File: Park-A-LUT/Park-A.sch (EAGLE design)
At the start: 38 parts, among them Q1 16MHz, T1 BC848SMD, T2 IRLML5203, T3 BC848SMD, T4 IRLML5203, U1 PIC18F25K80, U2 78M05, U3 TJA1055T

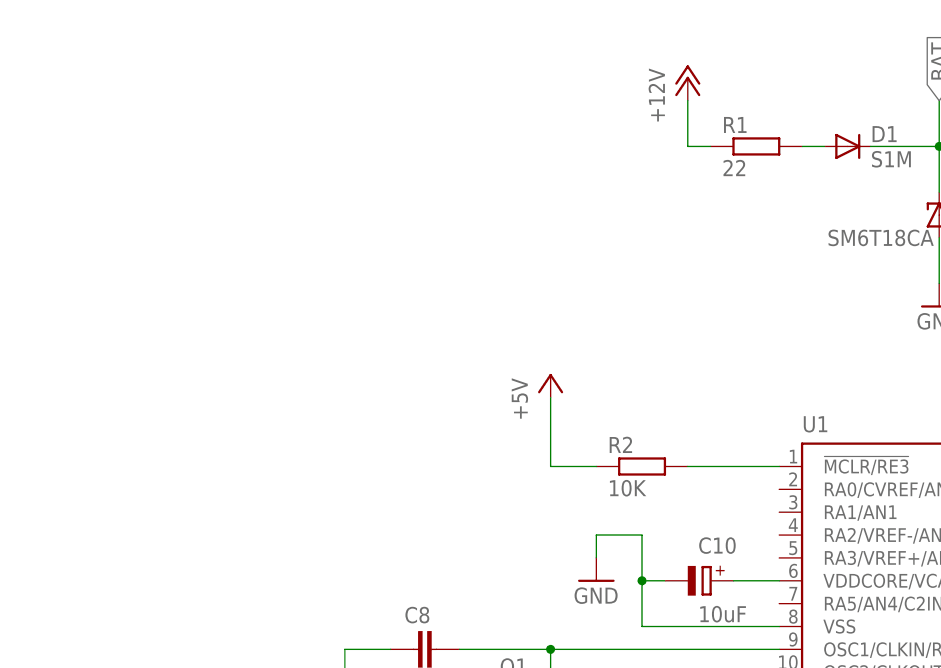
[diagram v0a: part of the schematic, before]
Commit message: Add ICSP
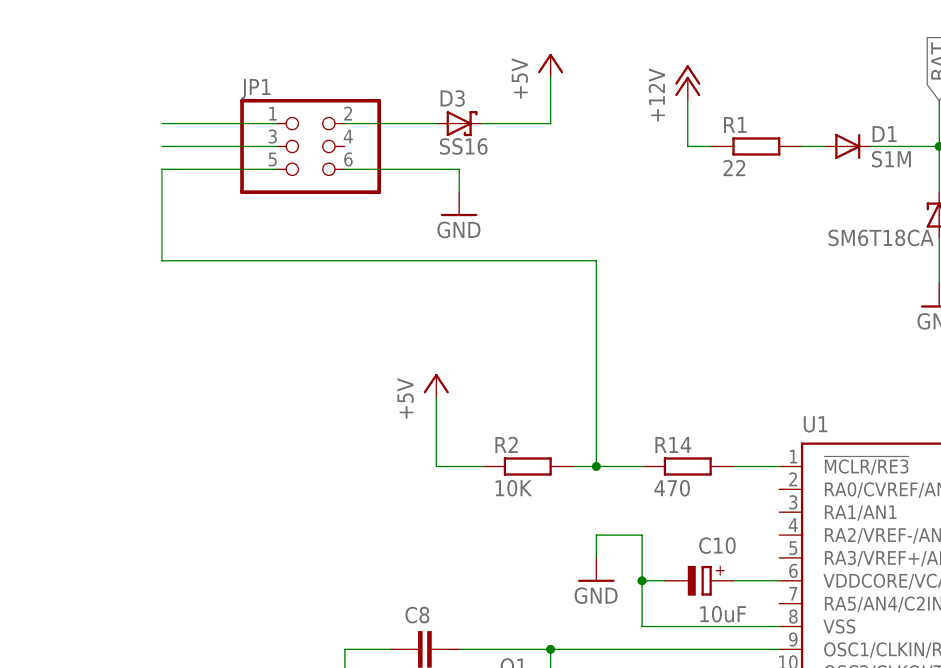
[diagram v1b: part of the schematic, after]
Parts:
- added D3: SS16, Park-A:SS16
- added JP1: (no value), Park-A:PINHD-2X3
- added R14: 470, rcl:R-EU_R0805
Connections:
- new net N$19: JP1.5, R14.1, R2.2
- new net N$20: D3.A, JP1.2
- net +5V: now also D3.C
- net GND: now also JP1.6
- net N$4: now also R14.2; no longer R2.2
- net PGC: now also JP1.1
- net PGD: now also JP1.3
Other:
- moved on the sheet: R2
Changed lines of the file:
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@@
 <part name="T4" library="Park-A" deviceset="IRLML5203" device=""/>
 <part name="GND12" library="supply1" deviceset="GND" device=""/>
+<part name="JP1" library="Park-A" deviceset="PINHD-2X3" device=""/>
+<part name="GND13" library="supply1" deviceset="GND" device=""/>
+<part name="R14" library="rcl" deviceset="R-EU_" device="R0805" value="470"/>
+<part name="D3" library="Park-A" deviceset="SS16" device=""/>
+<part name="P+6" library="supply1" deviceset="+5V" device=""/>
 </parts>
 <sheets>
@@
 <attribute name="NAME" x="86.36" y="-12.7" size="1.778" layer="94"/>
 </instance>
-<instance part="R2" gate="G$1" x="-83.82" y="-12.7"/>
-<instance part="P+3" gate="1" x="-93.98" y="-2.54"/>
+<instance part="R2" gate="G$1" x="-96.52" y="-12.7"/>
+<instance part="P+3" gate="1" x="-106.68" y="-2.54"/>
 <instance part="P+4" gate="1" x="73.66" y="-2.54"/>
 <instance part="GND3" gate="1" x="58.42" y="-45.72"/>
@@
 <instance part="T4" gate="G$1" x="86.36" y="-73.66"/>
 <instance part="GND12" gate="1" x="5.08" y="-93.98"/>
+<instance part="JP1" gate="A" x="-121.92" y="22.86"/>
+<instance part="GND13" gate="1" x="-104.14" y="15.24"/>
+<instance part="R14" gate="G$1" x="-78.74" y="-12.7"/>
+<instance part="D3" gate="G$1" x="-104.14" y="25.4"/>
+<instance part="P+6" gate="1" x="-93.98" y="33.02"/>
 </instances>
 <busses>
@@
 <wire x1="5.08" y1="-86.36" x2="5.08" y2="-91.44" width="0.1524" layer="91"/>
 </segment>
+<segment>
+<pinref part="JP1" gate="A" pin="6"/>
+<pinref part="GND13" gate="1" pin="GND"/>
+<wire x1="-116.84" y1="20.32" x2="-104.14" y2="20.32" width="0.1524" layer="91"/>
+<wire x1="-104.14" y1="20.32" x2="-104.14" y2="17.78" width="0.1524" layer="91"/>
+</segment>
 </net>
 <net name="+5V" class="0">
@@
 <segment>
 <pinref part="P+3" gate="1" pin="+5V"/>
-<wire x1="-93.98" y1="-5.08" x2="-93.98" y2="-12.7" width="0.1524" layer="91"/>
+<wire x1="-106.68" y1="-5.08" x2="-106.68" y2="-12.7" width="0.1524" layer="91"/>
 <pinref part="R2" gate="G$1" pin="1"/>
-<wire x1="-93.98" y1="-12.7" x2="-88.9" y2="-12.7" width="0.1524" layer="91"/>
+<wire x1="-106.68" y1="-12.7" x2="-101.6" y2="-12.7" width="0.1524" layer="91"/>
 </segment>
 <segment>
@@
 <junction x="114.3" y="-38.1"/>
 </segment>
+<segment>
+<pinref part="D3" gate="G$1" pin="C"/>
+<pinref part="P+6" gate="1" pin="+5V"/>
+<wire x1="-101.6" y1="25.4" x2="-93.98" y2="25.4" width="0.1524" layer="91"/>
+<wire x1="-93.98" y1="25.4" x2="-93.98" y2="30.48" width="0.1524" layer="91"/>
+</segment>
 </net>
 <net name="N$2" class="0">
@@
 <pinref part="U1" gate="G$1" pin="RC7/CANRX/RX1/DT1/CCP4"/>
 <wire x1="53.34" y1="-38.1" x2="22.86" y2="-38.1" width="0.1524" layer="91"/>
-</segment>
-</net>
-<net name="N$4" class="0">
-<segment>
-<pinref part="U1" gate="G$1" pin="!MCLR/RE3"/>
-<pinref part="R2" gate="G$1" pin="2"/>
-<wire x1="-68.58" y1="-12.7" x2="-78.74" y2="-12.7" width="0.1524" layer="91"/>
 </segment>
 </net>
@@
 <label x="27.94" y="7.62" size="1.778" layer="95" rot="R90" xref="yes"/>
 </segment>
+<segment>
+<pinref part="JP1" gate="A" pin="1"/>
+<wire x1="-124.46" y1="25.4" x2="-137.16" y2="25.4" width="0.1524" layer="91"/>
+</segment>
 </net>
 <net name="PGD" class="0">
@@
 <label x="25.4" y="0" size="1.778" layer="95" rot="R90" xref="yes"/>
 </segment>
-</net>
+<segment>
+<pinref part="JP1" gate="A" pin="3"/>
+<wire x1="-124.46" y1="22.86" x2="-137.16" y2="22.86" width="0.1524" layer="91"/>
+</segment>
+</net>
+<net name="N$19" class="0">
+<segment>
+<pinref part="JP1" gate="A" pin="5"/>
+<wire x1="-124.46" y1="20.32" x2="-137.16" y2="20.32" width="0.1524" layer="91"/>
+<wire x1="-137.16" y1="20.32" x2="-137.16" y2="10.16" width="0.1524" layer="91"/>
+<pinref part="R2" gate="G$1" pin="2"/>
+<wire x1="-88.9" y1="-12.7" x2="-91.44" y2="-12.7" width="0.1524" layer="91"/>
+<wire x1="-137.16" y1="10.16" x2="-88.9" y2="10.16" width="0.1524" layer="91"/>
+<wire x1="-88.9" y1="10.16" x2="-88.9" y2="-12.7" width="0.1524" layer="91"/>
+<pinref part="R14" gate="G$1" pin="1"/>
+<wire x1="-88.9" y1="-12.7" x2="-83.82" y2="-12.7" width="0.1524" layer="91"/>
+<junction x="-88.9" y="-12.7"/>
+</segment>
+</net>
+<net name="N$4" class="0">
+<segment>
+<pinref part="R14" gate="G$1" pin="2"/>
+<pinref part="U1" gate="G$1" pin="!MCLR/RE3"/>
+<wire x1="-73.66" y1="-12.7" x2="-68.58" y2="-12.7" width="0.1524" layer="91"/>
+</segment>
+</net>
+<net name="N$20" class="0">
+<segment>
+<pinref part="JP1" gate="A" pin="2"/>
+<pinref part="D3" gate="G$1" pin="A"/>
+<wire x1="-116.84" y1="25.4" x2="-106.68" y2="25.4" width="0.1524" layer="91"/>
+</segment>
+</net>

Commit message: Small fixes
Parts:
- added C11: 0.1uF, rcl:C-EUC0805
- renumbered JP1 to ICSP
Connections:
- removed net N$19: ICSP.5, R14.1, R2.2
- new net MCLR: ICSP.5, R14.2, U1.!MCLR/RE3
- net GND: now also C11.2
- net N$4: now also C11.1, R14.1, R2.2; no longer R14.2, U1.!MCLR/RE3
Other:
- moved on the sheet: R14, R2
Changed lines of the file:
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@@
 <part name="T4" library="Park-A" deviceset="IRLML5203" device=""/>
 <part name="GND12" library="supply1" deviceset="GND" device=""/>
-<part name="JP1" library="Park-A" deviceset="PINHD-2X3" device=""/>
+<part name="ICSP" library="Park-A" deviceset="PINHD-2X3" device=""/>
 <part name="GND13" library="supply1" deviceset="GND" device=""/>
-<part name="R14" library="rcl" deviceset="R-EU_" device="R0805" value="470"/>
 <part name="D3" library="Park-A" deviceset="SS16" device=""/>
 <part name="P+6" library="supply1" deviceset="+5V" device=""/>
+<part name="R14" library="rcl" deviceset="R-EU_" device="R0805" value="470"/>
+<part name="C11" library="rcl" deviceset="C-EU" device="C0805" value="0.1uF"/>
+<part name="GND14" library="supply1" deviceset="GND" device=""/>
 </parts>
 <sheets>
@@
 <attribute name="NAME" x="86.36" y="-12.7" size="1.778" layer="94"/>
 </instance>
-<instance part="R2" gate="G$1" x="-96.52" y="-12.7"/>
-<instance part="P+3" gate="1" x="-106.68" y="-2.54"/>
+<instance part="R2" gate="G$1" x="-124.46" y="-5.08" rot="R270"/>
+<instance part="P+3" gate="1" x="-124.46" y="5.08"/>
 <instance part="P+4" gate="1" x="73.66" y="-2.54"/>
 <instance part="GND3" gate="1" x="58.42" y="-45.72"/>
@@
 <instance part="T4" gate="G$1" x="86.36" y="-73.66"/>
 <instance part="GND12" gate="1" x="5.08" y="-93.98"/>
-<instance part="JP1" gate="A" x="-121.92" y="22.86"/>
+<instance part="ICSP" gate="A" x="-121.92" y="22.86"/>
 <instance part="GND13" gate="1" x="-104.14" y="15.24"/>
-<instance part="R14" gate="G$1" x="-78.74" y="-12.7"/>
 <instance part="D3" gate="G$1" x="-104.14" y="25.4"/>
 <instance part="P+6" gate="1" x="-93.98" y="33.02"/>
+<instance part="R14" gate="G$1" x="-96.52" y="-12.7"/>
+<instance part="C11" gate="G$1" x="-124.46" y="-20.32"/>
+<instance part="GND14" gate="1" x="-124.46" y="-30.48"/>
 </instances>
 <busses>
@@
 </segment>
 <segment>
-<pinref part="JP1" gate="A" pin="6"/>
+<pinref part="ICSP" gate="A" pin="6"/>
 <pinref part="GND13" gate="1" pin="GND"/>
 <wire x1="-116.84" y1="20.32" x2="-104.14" y2="20.32" width="0.1524" layer="91"/>
 <wire x1="-104.14" y1="20.32" x2="-104.14" y2="17.78" width="0.1524" layer="91"/>
+</segment>
+<segment>
+<pinref part="GND14" gate="1" pin="GND"/>
+<pinref part="C11" gate="G$1" pin="2"/>
+<wire x1="-124.46" y1="-27.94" x2="-124.46" y2="-25.4" width="0.1524" layer="91"/>
 </segment>
 </net>
@@
 <segment>
 <pinref part="P+3" gate="1" pin="+5V"/>
-<wire x1="-106.68" y1="-5.08" x2="-106.68" y2="-12.7" width="0.1524" layer="91"/>
+<wire x1="-124.46" y1="2.54" x2="-124.46" y2="0" width="0.1524" layer="91"/>
 <pinref part="R2" gate="G$1" pin="1"/>
-<wire x1="-106.68" y1="-12.7" x2="-101.6" y2="-12.7" width="0.1524" layer="91"/>
 </segment>
 <segment>
@@
 </segment>
 <segment>
-<pinref part="JP1" gate="A" pin="1"/>
+<pinref part="ICSP" gate="A" pin="1"/>
 <wire x1="-124.46" y1="25.4" x2="-137.16" y2="25.4" width="0.1524" layer="91"/>
+<label x="-137.16" y="25.4" size="1.778" layer="95" rot="R180" xref="yes"/>
 </segment>
 </net>
@@
 </segment>
 <segment>
-<pinref part="JP1" gate="A" pin="3"/>
-<wire x1="-124.46" y1="22.86" x2="-137.16" y2="22.86" width="0.1524" layer="91"/>
-</segment>
-</net>
-<net name="N$19" class="0">
-<segment>
-<pinref part="JP1" gate="A" pin="5"/>
-<wire x1="-124.46" y1="20.32" x2="-137.16" y2="20.32" width="0.1524" layer="91"/>
-<wire x1="-137.16" y1="20.32" x2="-137.16" y2="10.16" width="0.1524" layer="91"/>
-<pinref part="R2" gate="G$1" pin="2"/>
-<wire x1="-88.9" y1="-12.7" x2="-91.44" y2="-12.7" width="0.1524" layer="91"/>
-<wire x1="-137.16" y1="10.16" x2="-88.9" y2="10.16" width="0.1524" layer="91"/>
-<wire x1="-88.9" y1="10.16" x2="-88.9" y2="-12.7" width="0.1524" layer="91"/>
-<pinref part="R14" gate="G$1" pin="1"/>
-<wire x1="-88.9" y1="-12.7" x2="-83.82" y2="-12.7" width="0.1524" layer="91"/>
-<junction x="-88.9" y="-12.7"/>
-</segment>
-</net>
-<net name="N$4" class="0">
-<segment>
+<pinref part="ICSP" gate="A" pin="3"/>
+<wire x1="-124.46" y1="22.86" x2="-147.32" y2="22.86" width="0.1524" layer="91"/>
+<label x="-147.32" y="22.86" size="1.778" layer="95" rot="R180" xref="yes"/>
+</segment>
+</net>
+<net name="MCLR" class="0">
+<segment>
+<wire x1="-76.2" y1="-7.62" x2="-76.2" y2="-12.7" width="0.1524" layer="91"/>
+<pinref part="U1" gate="G$1" pin="!MCLR/RE3"/>
+<wire x1="-76.2" y1="-12.7" x2="-68.58" y2="-12.7" width="0.1524" layer="91"/>
 <pinref part="R14" gate="G$1" pin="2"/>
-<pinref part="U1" gate="G$1" pin="!MCLR/RE3"/>
-<wire x1="-73.66" y1="-12.7" x2="-68.58" y2="-12.7" width="0.1524" layer="91"/>
+<wire x1="-91.44" y1="-12.7" x2="-76.2" y2="-12.7" width="0.1524" layer="91"/>
+<junction x="-76.2" y="-12.7"/>
+<label x="-76.2" y="-7.62" size="1.778" layer="95" rot="R90" xref="yes"/>
+</segment>
+<segment>
+<pinref part="ICSP" gate="A" pin="5"/>
+<wire x1="-124.46" y1="20.32" x2="-132.08" y2="20.32" width="0.1524" layer="91"/>
+<label x="-132.08" y="20.32" size="1.778" layer="95" rot="R180" xref="yes"/>
 </segment>
 </net>
 <net name="N$20" class="0">
 <segment>
-<pinref part="JP1" gate="A" pin="2"/>
+<pinref part="ICSP" gate="A" pin="2"/>
 <pinref part="D3" gate="G$1" pin="A"/>
 <wire x1="-116.84" y1="25.4" x2="-106.68" y2="25.4" width="0.1524" layer="91"/>
 </segment>
 </net>
+<net name="N$4" class="0">
+<segment>
+<pinref part="R2" gate="G$1" pin="2"/>
+<wire x1="-124.46" y1="-12.7" x2="-124.46" y2="-10.16" width="0.1524" layer="91"/>
+<pinref part="R14" gate="G$1" pin="1"/>
+<wire x1="-124.46" y1="-12.7" x2="-101.6" y2="-12.7" width="0.1524" layer="91"/>
+<pinref part="C11" gate="G$1" pin="1"/>
+<wire x1="-124.46" y1="-17.78" x2="-124.46" y2="-12.7" width="0.1524" layer="91"/>
+<junction x="-124.46" y="-12.7"/>
+</segment>
+</net>
